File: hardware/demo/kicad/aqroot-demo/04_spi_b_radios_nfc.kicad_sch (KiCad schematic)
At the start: 44 parts, among them J7 BM02B-ACHSS-GAN-ETF, U7 E07-400M10S, U8 E22-900M22S, U9 ST25R3916-AQET, Y1 27.12MHz 10pF 3225-4P

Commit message: demo: the BOM is THREE QUARTERS orderable -- 122 part identities grafted from prior CTO audits, every one re-read off the PART instead of the line, and four gates that had never been run (D-614)
NO COPPER CHANGED.  The authoritative board is byte-identical at
c8e421aa50144fe396aedb5e226aaabeb815bd69ffaf6e04f549ded43831d103 and 26 of the
package's 28 artifacts are normalised-sha-identical to D-613's; the two that
moved are the two BOM views.

FAB7 coverage 25.9% -> 75.3%, orderable references 64 -> 186 of 247.
36 BOM lines / 122 references gained Manufacturer / MPN / LCSC -- 487 properties
across nine schematic sheets, replayable to byte-identical sheets.

Four things the mechanical answer would have got wrong: a REJECTED audit row's
JLC Manufacturer column names the match that was THROWN OUT (16 of 31 grafts);
the rating belongs to the PART, not the line; the designator is not the
identity; and the beta-dm 0 ohm current gate had never been run on five of the
Demo's eight links.

Two defects in the instruments fixed: the value parser could not read 15mR, and
MANIFEST.json hashed only the ROOT schematic sheet while nine child sheets
changed.

Re-proved on this tree: verify_promotion.py 14/14, FAB1-FAB6 + FAB8 PASS,
POP1-POP4, P1-P4, protected copper 15 nets / 393 objects IDENTICAL.
FAB7 still FAILS and is partitioned: 8 lines / 16 parts TUNE, 26 lines /
45 parts genuinely open.

Co-Authored-By: Claude Opus 5 <noreply@anthropic.com>
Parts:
- C16, C17: LCSC (none) -> C14663; MPN (none) -> CC0603KRX7R9BB104; Manufacturer (none) -> YAGEO; Note_Sourcing (none) -> SOURCING D-614. EXACT_PRIOR from the beta-dm audit line '10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
- C18, C19: LCSC (none) -> C105883; MPN (none) -> CC0402KRX7R8BB104; Manufacturer (none) -> YAGEO; Note_Sourcing (none) -> SOURCING D-614. EXACT_PRIOR from the beta-dm audit line '10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
- C53: LCSC (none) -> C15849; MPN (none) -> CL10A105KB8NNNC; Manufacturer (none) -> Samsung Electro-Mechanics; Note_Sourcing (none) -> SOURCING D-614. EXACT_PRIOR from the beta-dm audit line '1u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
- R27, R28, R29: LCSC (none) -> C25804; MPN (none) -> 0603WAF1002T5E; Manufacturer (none) -> UNI-ROYAL(Uniroyal Elec); Note_Sourcing (none) -> SOURCING D-614. EXACT_PRIOR from the beta-dm audit line '10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
- R74: LCSC (none) -> C25803; MPN (none) -> 0603WAF1003T5E; Manufacturer (none) -> UNI-ROYAL(Uniroyal Elec); Note_Sourcing (none) -> SOURCING D-614. EXACT_PRIOR from the beta-dm audit line '10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

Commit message: demo: the BOM is 100% ORDERABLE and the safety part was ordered in the WRONG PACKAGE -- 61 identities ruled against a live distributor record, and a screen that asks the C26 question of every line at once (D-615)
D-614 named this task and named what stopped it: D-096 binds -- a part number
configured from an ordering scheme is a hypothesis until a distributor record
confirms lifecycle and stock, and that session had none to read.  This one read
the JLCPCB catalogue 225 times and KEPT every answer, each stamped with the UTC
minute it was read.

NO COPPER CHANGED.  The authoritative board is byte-identical at
c8e421aa50144fe396aedb5e226aaabeb815bd69ffaf6e04f549ded43831d103.

FAB7 IS CLOSED.  Coverage 75.3% -> 100.0%, orderable 186 -> 247 of 247,
needs_a_sourcing_decision ZERO lines, and fab_package_contract.py reads
FAB1-FAB8 PASS for the first time.

THE FINDING.  screen_part_land_parity.py asks D-613's C26 question of every
sourced line at once against the catalogue's own package field: 119 lines carry
a code, 75 are comparable, 74 MATCH and U18 did not.  The land is MSOP-10; the
BOM ordered LTC4368IDD-1#PBF, and DD is DFN-10-EP(3x3) -- against D-099, which
locked LTC4368IMS-1#PBF under FBV2-PWR-002's "no bottom-terminated parts" on
the single most safety-critical component.  The cached library symbol AND the
project .kicad_sym both still carried it, with a Package field describing a DFN
beside a Footprint field already reading MSOP-10.  Corrected to
LTC4368IMS-1#TRPBF, LCSC C688401 -- the tape-and-reel order code of the
identical device, D-210's precedent, not an electrical change.

Three things the obvious answer would have got wrong: R69 is 1.87 ohm and its
part is 0603WAF187KT5E while 0603WAF1873T5E is 187 kOhm; R95's node over-bound
UNDERSTATES its dissipation because a reversed cell adds in series (154 mW vs
54 mW); and R24/C12's Value strings are looser than their own symbol notes.
NET_MAX_DC grew 17 -> 48 established nodes to give the new dissipation gate
nu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
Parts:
- C45, C47, C49, C51: LCSC (none) -> C125847; MPN (none) -> CC0805KKX7R9BB225; Manufacturer (none) -> YAGEO; Note_Sourcing (none) -> SOURCING D-615 LIVE_RECORD. JLCPCB record read 2026-09-05T0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
- C46, C48, C50, C54: LCSC (none) -> C57112; MPN (none) -> 0603B103K500NT; Manufacturer (none) -> FH (Guangdong Fenghua Advanced Tech); Note_Sourcing (none) -> SOURCING D-615 LIVE_RECORD. JLCPCB record read 2026-09-05T0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
- C52: LCSC (none) -> C1588; MPN (none) -> CL10B102KB8NNNC; Manufacturer (none) -> Samsung Electro-Mechanics; Note_Sourcing (none) -> SOURCING D-615 LIVE_RECORD. JLCPCB record read 2026-09-05T0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
- C55: LCSC (none) -> C23630; MPN (none) -> CL10A225KO8NNNC; Manufacturer (none) -> Samsung Electro-Mechanics; Note_Sourcing (none) -> SOURCING D-615 LIVE_RECORD. JLCPCB record read 2026-09-05T0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
- C69, C70: LCSC (none) -> C14858; MPN (none) -> CL10C101JB8NNNC; Manufacturer (none) -> Samsung Electro-Mechanics; Note_Sourcing (none) -> FIRST-ARTICLE VALUE ONLY -- DEVICE_SPEC s.14 requires this 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
- C71, C72: LCSC (none) -> C3837533; MPN (none) -> GCM1885C2A301FA16J; Manufacturer (none) -> Murata Electronics; Note_Sourcing (none) -> FIRST-ARTICLE VALUE ONLY -- DEVICE_SPEC s.14 requires this 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
- C73, C74: LCSC (none) -> C388906; MPN (none) -> GCM1885C2A152JA16D; Manufacturer (none) -> Murata Electronics; Note_Sourcing (none) -> FIRST-ARTICLE VALUE ONLY -- DEVICE_SPEC s.14 requires this 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
- C75, C77: LCSC (none) -> C2360423; MPN (none) -> GQM1875C2E270FB12D; Manufacturer (none) -> Murata Electronics; Note_Sourcing (none) -> FIRST-ARTICLE VALUE ONLY -- DEVICE_SPEC s.14 requires this 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
- C76, C78: LCSC (none) -> C325470; MPN (none) -> CC0603JRNPO9BN621; Manufacturer (none) -> YAGEO; Note_Sourcing (none) -> FIRST-ARTICLE VALUE ONLY -- DEVICE_SPEC s.14 requires this 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
- C79, C80: LCSC (none) -> C1634; MPN (none) -> CL10C100JB8NNNC; Manufacturer (none) -> Samsung Electro-Mechanics; Note_Sourcing (none) -> FIRST-ARTICLE VALUE ONLY -- DEVICE_SPEC s.14 requires this 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
- R114, R115: LCSC (none) -> C309559; MPN (none) -> RC0603FR-071R1L; Manufacturer (none) -> YAGEO; Note_Sourcing (none) -> FIRST-ARTICLE VALUE ONLY -- DEVICE_SPEC s.14 requires this 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
- R116, R117: LCSC (none) -> C21190; MPN (none) -> 0603WAF1001T5E; Manufacturer (none) -> UNI-ROYAL(Uniroyal Elec); Note_Sourcing (none) -> FIRST-ARTICLE VALUE ONLY -- DEVICE_SPEC s.14 requires this 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

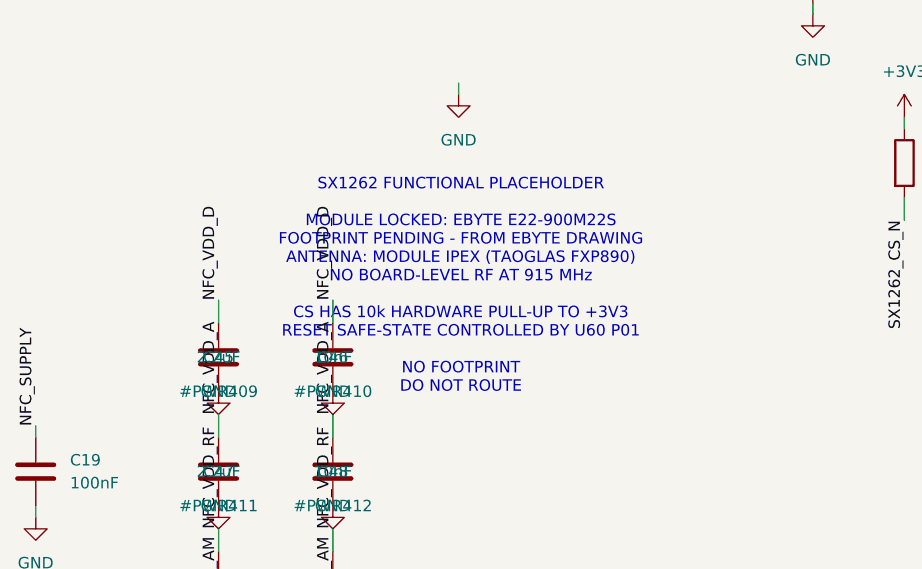
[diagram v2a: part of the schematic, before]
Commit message: demo: D-769 -- the other superseded part name, and the clause that now refuses the whole class
authority 5849b658, UNCHANGED.  No PCB change and no copper of any kind.

D-768 section 7 deliberately left this one out rather than bundling it, and it
is the same defect.  U8's Package field said "Antenna: module IPEX/u.FL with
Taoglas FXP890.07.0100C", the sheet module note said "ANTENNA: MODULE IPEX
(TAOGLAS FXP890)", and ARCHITECTURE.md's 915 MHz row said "Taoglas FXP890 flex"
-- all naming the INTERNAL flex antenna that D-198 SUPERSEDED, and DEVICE_SPEC
had carried an explicit "This is STALE" note about those exact fields as an open
item.

THE CONSEQUENCE IF BELIEVED IS CONCRETE.  An FXP890 is an internal flex with a
u.FL/MHF-I connector.  Procuring it instead of the SMA whip and its
CBA-UFLSMA20IP pigtail leaves the 915 MHz radio with NO ANTENNA PATH THIS
PRODUCT SUPPORTS: the enclosure has a 6.5 mm top-panel bulkhead hole for a
screw-on whip and no internal volume or mounting provision for a flex.  All
three places now name the locked EXTERNAL Taoglas TI.92.2113 SMA(M) dipole
reached through module IPEX -> CBA-UFLSMA20IP pigtail -> top-panel SMA(F)
bulkhead.

AND F7 BECAME A REGISTRY RATHER THAN A SPECIAL CASE, because D-768 built it for
ONE reference and that is exactly the mistake D-767 named: a fix that closes one
instance and leaves the class open is half a fix.  F7 now holds J1 (retires
CH280QV10 / ILI9341 / 2.8in / 240x320) and U8 (retires FXP890), every entry a
supersession this repository had ALREADY recorded -- nothing inferred, and a
part with no recorded supersession is out of scope and the report says so.  For
each reference it asserts the locked identity in the placed symbol's lib_id, in
every property of the instance AND its library definition, AND on the released
BOM row; text explicitly ABOUT the retirement is exempt, which is what lets the
two RETIRED -- DO NOT INSTANTIATE annotations coexist with the rule.

Four live controls, all refused: the sta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
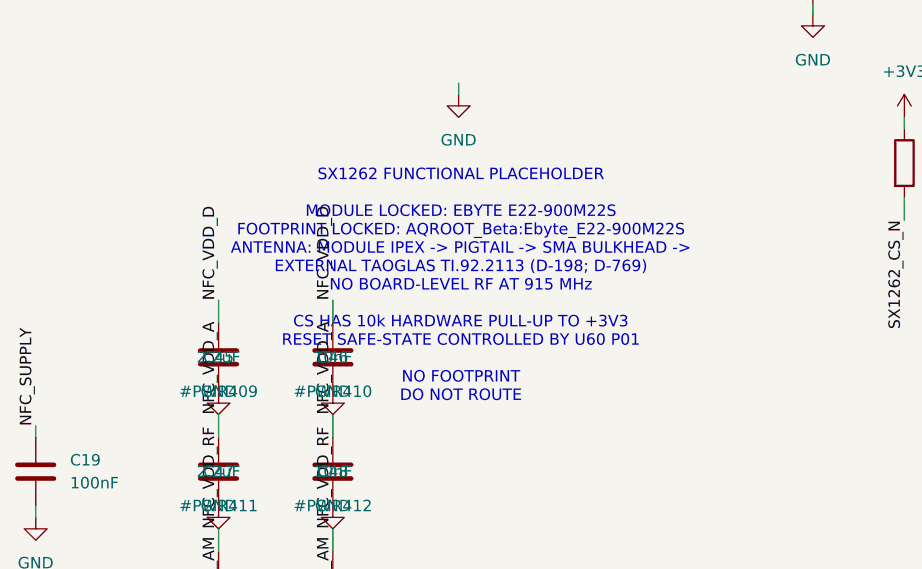
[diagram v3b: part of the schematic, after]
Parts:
- U8: Package 20.0 x 14.0 x 3.0 mm castellated module, 22 pads, 1.27 mm pitch with a 5.57 mm gap at the IPEX end. DIO2 (8) strapped locally to TXEN (7) - firmware MUST enable SX1262 SetDIO2AsRfSwitchCtrl. RXEN (6) driven from SX1262_RXEN on the reclaimed U3.19 expander port with a 100k pulldown for a defined CLOSE state. Antenna: module IPEX/u.FL with Taoglas FXP890.07.0100C; pin 21 ANT stamp hole present but NOT routed - RF DO NOT ROUTE until final RF review. Procurement: Beta units must ship with the IPEX connector populated. -> 20.0 x 14.0 x 3.0 mm castellated module, 22 pads, 1.27 mm pitch with a 5.57 mm gap at the IPEX end. DIO2 (8) strapped locally to TXEN (7) - firmware MUST enable SX1262 SetDIO2AsRfSwitchCtrl. RXEN (6) driven from SX1262_RXEN on the reclaimed U3.19 expander port with a 100k pulldown for a defined CLOSE state. Antenna: module IPEX/u.FL -> CBA-UFLSMA20IP pigtail -> top-panel SMA(F) bulkhead -> EXTERNAL Taoglas TI.92.2113 SMA(M) dipole, LOCKED by D-198; pin 21 ANT stamp hole present but NOT routed, and by design NO 433/915 RF signal reaches the main PCB. D-769 CORRECTED THIS FIELD: it named an internal Taoglas FXP890.07.0100C flex, which D-198 superseded and which DEVICE_SPEC has flagged STALE since -- procuring it instead of the SMA whip and pigtail would leave the 915 MHz radio with no antenna path this board supports. Procurement: Beta units must ship with the IPEX connector populated.
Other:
- note added: "SX1262 FUNCTIONAL PLACEHOLDER MODULE LOCKED: EBYTE E22-900M22S FOOTPRINT LOCKED: AQROOT_Beta:Ebyte_E22-900M22S ANTENNA: MODULE IPEX -> PIGTAIL -> SMA BULKHEAD -> EXTERNAL TAOGLAS TI.92.2113 (D-198; D-769) NO BOARD-LEVEL RF AT 915 MHz CS HAS 10k HARDWARE PULL-UP TO +3V3 RESET SAFE-STATE CONTROLLED BY U60 P01 NO FOOTPRINT DO NOT ROUTE"
- note removed: "SX1262 FUNCTIONAL PLACEHOLDER MODULE LOCKED: EBYTE E22-900M22S FOOTPRINT PENDING - FROM EBYTE DRAWING ANTENNA: MODULE IPEX (TAOGLAS FXP890) NO BOARD-LEVEL RF AT 915 MHz CS HAS 10k HARDWARE PULL-UP TO +3V3 RESET SAFE-STATE CONTROLLED BY U60 P01 NO FOOTPRINT DO NOT ROUTE"
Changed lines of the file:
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@@
 		)
 	)
-	(text "SX1262 FUNCTIONAL PLACEHOLDER\n\nMODULE LOCKED: EBYTE E22-900M22S\nFOOTPRINT PENDING - FROM EBYTE DRAWING\nANTENNA: MODULE IPEX (TAOGLAS FXP890)\nNO BOARD-LEVEL RF AT 915 MHz\n\nCS HAS 10k HARDWARE PULL-UP TO +3V3\nRESET SAFE-STATE CONTROLLED BY U60 P01\n\nNO FOOTPRINT\nDO NOT ROUTE"
+	(text "SX1262 FUNCTIONAL PLACEHOLDER\n\nMODULE LOCKED: EBYTE E22-900M22S\nFOOTPRINT LOCKED: AQROOT_Beta:Ebyte_E22-900M22S\nANTENNA: MODULE IPEX -> PIGTAIL -> SMA BULKHEAD ->\nEXTERNAL TAOGLAS TI.92.2113 (D-198; D-769)\nNO BOARD-LEVEL RF AT 915 MHz\n\nCS HAS 10k HARDWARE PULL-UP TO +3V3\nRESET SAFE-STATE CONTROLLED BY U60 P01\n\nNO FOOTPRINT\nDO NOT ROUTE"
 		(exclude_from_sim no)
 		(at 217.424 112.776 0)
@@
 			)
 		)
-		(property "Package" "20.0 x 14.0 x 3.0 mm castellated module, 22 pads, 1.27 mm pitch with a 5.57 mm gap at the IPEX end. DIO2 (8) strapped locally to TXEN (7) - firmware MUST enable SX1262 SetDIO2AsRfSwitchCtrl. RXEN (6) driven from SX1262_RXEN on the reclaimed U3.19 expander port with a 100k pulldown for a defined CLOSE state. Antenna: module IPEX/u.FL with Taoglas FXP890.07.0100C; pin 21 ANT stamp hole present but NOT routed - RF DO NOT ROUTE until final RF review. Procurement: Beta units must ship with the IPEX connector populated."
+		(property "Package" "20.0 x 14.0 x 3.0 mm castellated module, 22 pads, 1.27 mm pitch with a 5.57 mm gap at the IPEX end. DIO2 (8) strapped locally to TXEN (7) - firmware MUST enable SX1262 SetDIO2AsRfSwitchCtrl. RXEN (6) driven from SX1262_RXEN on the reclaimed U3.19 expander port with a 100k pulldown for a defined CLOSE state. Antenna: module IPEX/u.FL -> CBA-UFLSMA20IP pigtail -> top-panel SMA(F) bulkhead -> EXTERNAL Taoglas TI.92.2113 SMA(M) dipole, LOCKED by D-198; pin 21 ANT stamp hole present but NOT routed, and by design NO 433/915 RF signal reaches the main PCB. D-769 CORRECTED THIS FIELD: it named an internal Taoglas FXP890.07.0100C flex, which D-198 superseded and which DEVICE_SPEC has flagged STALE since -- procuring it instead of the SMA whip and pigtail would leave the 915 MHz radio with no antenna path this board supports. Procurement: Beta units must ship with the IPEX connector populated."
 			(at 217.17 63.5 0)
 			(hide yes)
